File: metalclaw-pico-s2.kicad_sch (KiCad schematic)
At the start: 3 parts, among them J1 USB_C_Receptacle_USB2.0_14P, U1 ESP32-S2, U2 W25Q16JVSS

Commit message: Initial schematic connections
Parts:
- added A2: RaspberryPi_Pico, Module:RaspberryPi_Pico_SMD_HandSolder, symbol MCU_Module:RaspberryPi_Pico_Debug
- added C1, C2, C3: C, symbol Device:C
- added R1, R29, R30, R31, R32, R33, R34, R35: 5.1k, symbol Device:R_US
- added R10, R11, R12, R13, R14, R15, R16, R17, R18, R19, R2, R20, R21, R22, R23, R24, R25, R26, R27, R28, R3, R4, R5, R6, R7, R8, R9: R_US, symbol Device:R_US
- added U3: APS6404L-3SQRx-SN, Package_SO:SOIC-8_3.9x4.9mm_P1.27mm, symbol Memory_RAM:APS6404L-3SQRx-SN
- added U4: AMS1117-3.3, Package_TO_SOT_SMD:SOT-223-3_TabPin2, symbol Regulator_Linear:AMS1117-3.3
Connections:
- net GND: now also U1.57 (GND), U2.4 (GND), A2.13 (GND), A2.18 (GND), A2.23 (GND), A2.28 (GND), A2.3 (GND), A2.33 (AGND), A2.38 (GND), A2.8 (GND), A2.D2 (GND), C1.2, C2.2, C3.2, R1.1, R29.1, R30.1, R31.1, U3.4 (VSS), U4.1 (GND)
- net VBUS: now reaches J1.A4 (VBUS), J1.A9 (VBUS), J1.B4 (VBUS), J1.B9 (VBUS)
- net VBUS: now also A2.40 (VBUS), C1.1, U4.3 (VI)
- net at J1.A5 (CC1): now also R1.2
- net at J1.A6 (D+), U1.26 (GPIO20/USB_D+): no longer J1.B6 (D+)
- net at J1.B5 (CC2): now also R29.2
- net GP4: now reaches U1.10 (GPIO5)
- net GP4: now also R6.2
- net GP5: now reaches U1.11 (GPIO6)
- net GP5: now also R7.2
- net GP6: now reaches U1.12 (GPIO7)
- net GP6: now also R18.2, R34.2
- net GP7: now reaches U1.13 (GPIO8)
- net GP7: now also R19.2, R35.2
- net GP8: now reaches U1.14 (GPIO9)
- net GP8: now also R20.2
- net GP9: now reaches U1.15 (GPIO10)
- net GP9: now also R21.2
- net GP10: now reaches U1.16 (GPIO11)
- net GP10: now also R22.2
- net GP11: now reaches U1.17 (GPIO12)
- net GP11: now also R23.2
- net GP12: now reaches U1.18 (GPIO13)
- net GP12: now also R24.2
- net GP13: now reaches U1.19 (GPIO14)
- net GP13: now also R25.2
- net GP14: now reaches U1.21 (XTAL_32K_P)
- net GP14: now also R26.2
- net GP15: now reaches U1.22 (XTAL_32K_N)
- net GP15: now also R27.2
- net GP26: now reaches U1.23 (DAC_1)
- net GP26: now also R8.2
- net GP27: now reaches U1.24 (DAC_2)
- net GP27: now also R16.2
- net at U1.28 (GPIO21): now also R28.1
- net at U1.29 (SPICS1): now also U3.1 (~{CE})
- net at U1.31 (SPIHD), U2.7 (~{HOLD}/~{RESET}/IO_{3}): now also U3.3 (SIO2)
- net at U1.32 (SPIWP), U2.3 (~{WP}/IO_{2}): now also U3.7 (SIO3)
- net at U1.34 (SPICLK), U2.6 (CLK): now also U3.6 (SCLK)
- net at U1.35 (SPIQ): now also U2.5 (DI/IO_{0}), U3.5 (SI/SIO0)
- net at U1.36 (SPID): now also U2.2 (DO/IO_{1}), U3.2 (SO/SIO1)
- net GP16: now reaches U1.37 (GPIO33)
- net GP16: now also R15.2
- net GP17: now reaches U1.38 (GPIO34)
- net GP17: now also R14.2
- net GP18: now reaches U1.39 (GPIO35)
- net GP18: now also R13.2
- net GP19: now reaches U1.40 (GPIO36)
- net GP19: now also R12.2
- net GP21: now reaches U1.41 (GPIO37)
- net GP21: now also R10.2, R33.2
- net GP20: now reaches U1.42 (GPIO38)
- net GP20: now also R11.2, R32.2
- net SWCLK: now reaches U1.48 (U0TXD)
- net SWCLK: now also A2.D1 (SWCLK)
- net SWDIO: now reaches U1.49 (U0RXD)
- net SWDIO: now also A2.D3 (SWDIO)
- net RUN: now reaches U1.5 (GPIO0)
- net RUN: now also A2.30 (RUN)
- net 3V3_EN: now reaches U1.50 (GPIO45)
- net 3V3_EN: now also A2.37 (3V3_EN), R30.2
- net GP22: now reaches U1.55 (GPIO46)
- net GP22: now also R31.2, R9.2
- net GP0: now reaches U1.6 (GPIO1)
- net GP0: now also R2.2
- net GP1: now reaches U1.7 (GPIO2)
- net GP1: now also R3.2
- net GP2: now reaches U1.8 (GPIO3)
- net GP2: now also R4.2
- net GP3: now reaches U1.9 (GPIO4)
- net GP3: now also R5.2
- net +3.3V: now reaches U2.8 (VCC)
- net +3.3V: now also U3.8 (VDD)
- new net: A2.16 (GPIO12), R24.1
- new net: A2.1 (GPIO0), R2.1
- new net: A2.10 (GPIO7), R19.1
- new net: A2.11 (GPIO8), R20.1
- new net: A2.12 (GPIO9), R21.1
- new net: A2.14 (GPIO10), R22.1
- new net: A2.15 (GPIO11), R23.1
- new net: A2.17 (GPIO13), R25.1
- new net: A2.19 (GPIO14), R26.1
- new net: A2.2 (GPIO1), R3.1
- new net: A2.20 (GPIO15), R27.1
- new net: A2.21 (GPIO16), R15.1
- new net: A2.22 (GPIO17), R14.1
- new net: A2.24 (GPIO18), R13.1
- new net: A2.25 (GPIO19), R12.1
- new net: A2.26 (GPIO20), R11.1
- new net: A2.27 (GPIO21), R10.1
- new net: A2.29 (GPIO22), R9.1
- new net: A2.31 (GPIO26_ADC0), R8.1
- new net: A2.32 (GPIO27_ADC1), R16.1
- new net: A2.34 (GPIO28_ADC2), R17.1
- new net: A2.4 (GPIO2), R4.1
- new net: A2.5 (GPIO3), R5.1
- new net: A2.6 (GPIO4), R6.1
- new net: A2.7 (GPIO5), R7.1
- new net: A2.9 (GPIO6), R18.1
- new net +3V3: A2.35 (ADC_VREF), A2.36 (3V3), C3.1, R32.1, R33.1, R34.1, R35.1, U4.2 (VO)
- new net GP28: C2.1, J1.B6 (D+), R17.2, R28.2
- new net VS: A2.39 (VSYS)
- no-connect marks 1 -> 2
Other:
- moved on the sheet: J1, U1, U2

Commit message: Switch 3V3_EN and RUN pins
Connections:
- net 3V3_EN: now also U1.5 (GPIO0); no longer R30.2, U1.50 (GPIO45)
- net RUN: now also R30.2, U1.50 (GPIO45); no longer U1.5 (GPIO0)
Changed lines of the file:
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@@
 	)
 	(label "3V3_EN"
-		(at 121.92 53.34 270)
+		(at 71.12 147.32 90)
 		(effects
 			(font
 				(size 1.27 1.27)
 			)
-			(justify right bottom)
+			(justify left bottom)
 		)
 	)
@@
 	)
 	(label "RUN"
-		(at 71.12 147.32 90)
+		(at 121.92 53.34 270)
 		(effects
 			(font
 				(size 1.27 1.27)
 			)
-			(justify left bottom)
+			(justify right bottom)
 		)
 	)

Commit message: Specify series resistor resistance and footprint
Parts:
- removed R17: R_US, symbol Device:R_US
- R1, R29, R30, R31, R32, R33, R34, R35: footprint (none) -> Capacitor_SMD:C_0402_1005Metric
- R10, R11, R12, R13, R14, R15, R16, R18, R19, R2, R20, R21, R22, R23, R24, R25, R26, R27, R28, R3, R4, R5, R6, R7, R8, R9: value R_US -> 220; footprint (none) -> Capacitor_SMD:C_0402_1005Metric
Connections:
- net GP28: now also A2.34 (GPIO28_ADC2)

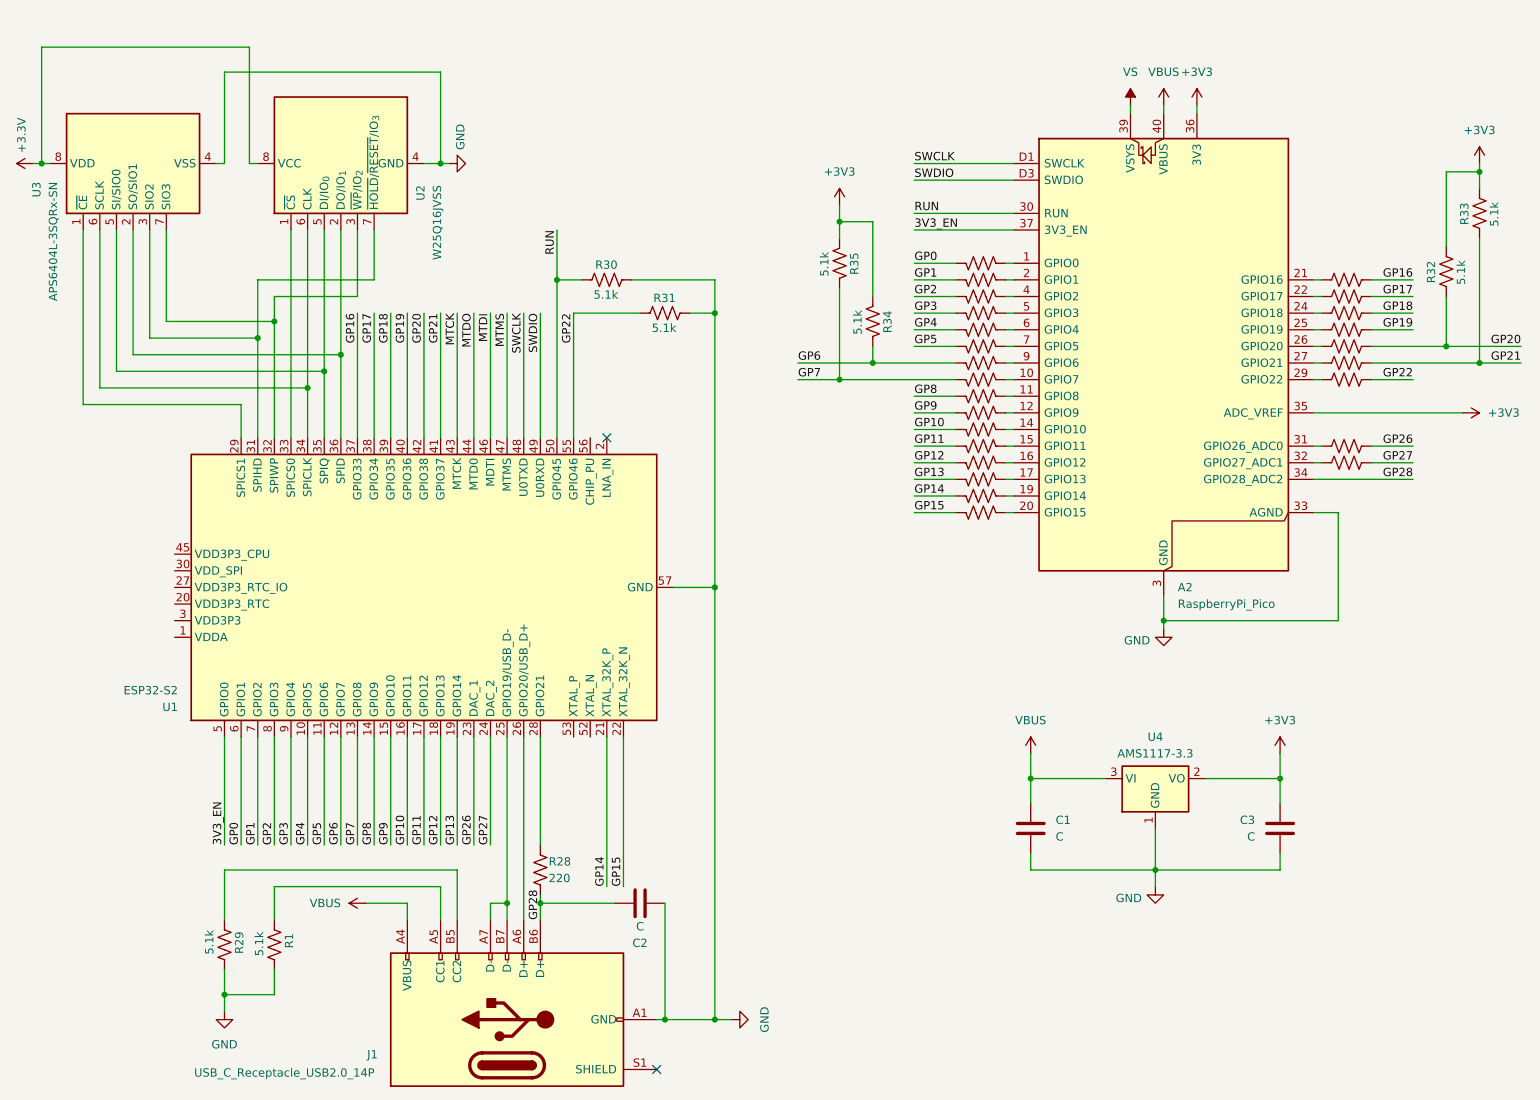
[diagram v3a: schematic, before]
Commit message: Add cap banks to ESP32-S2
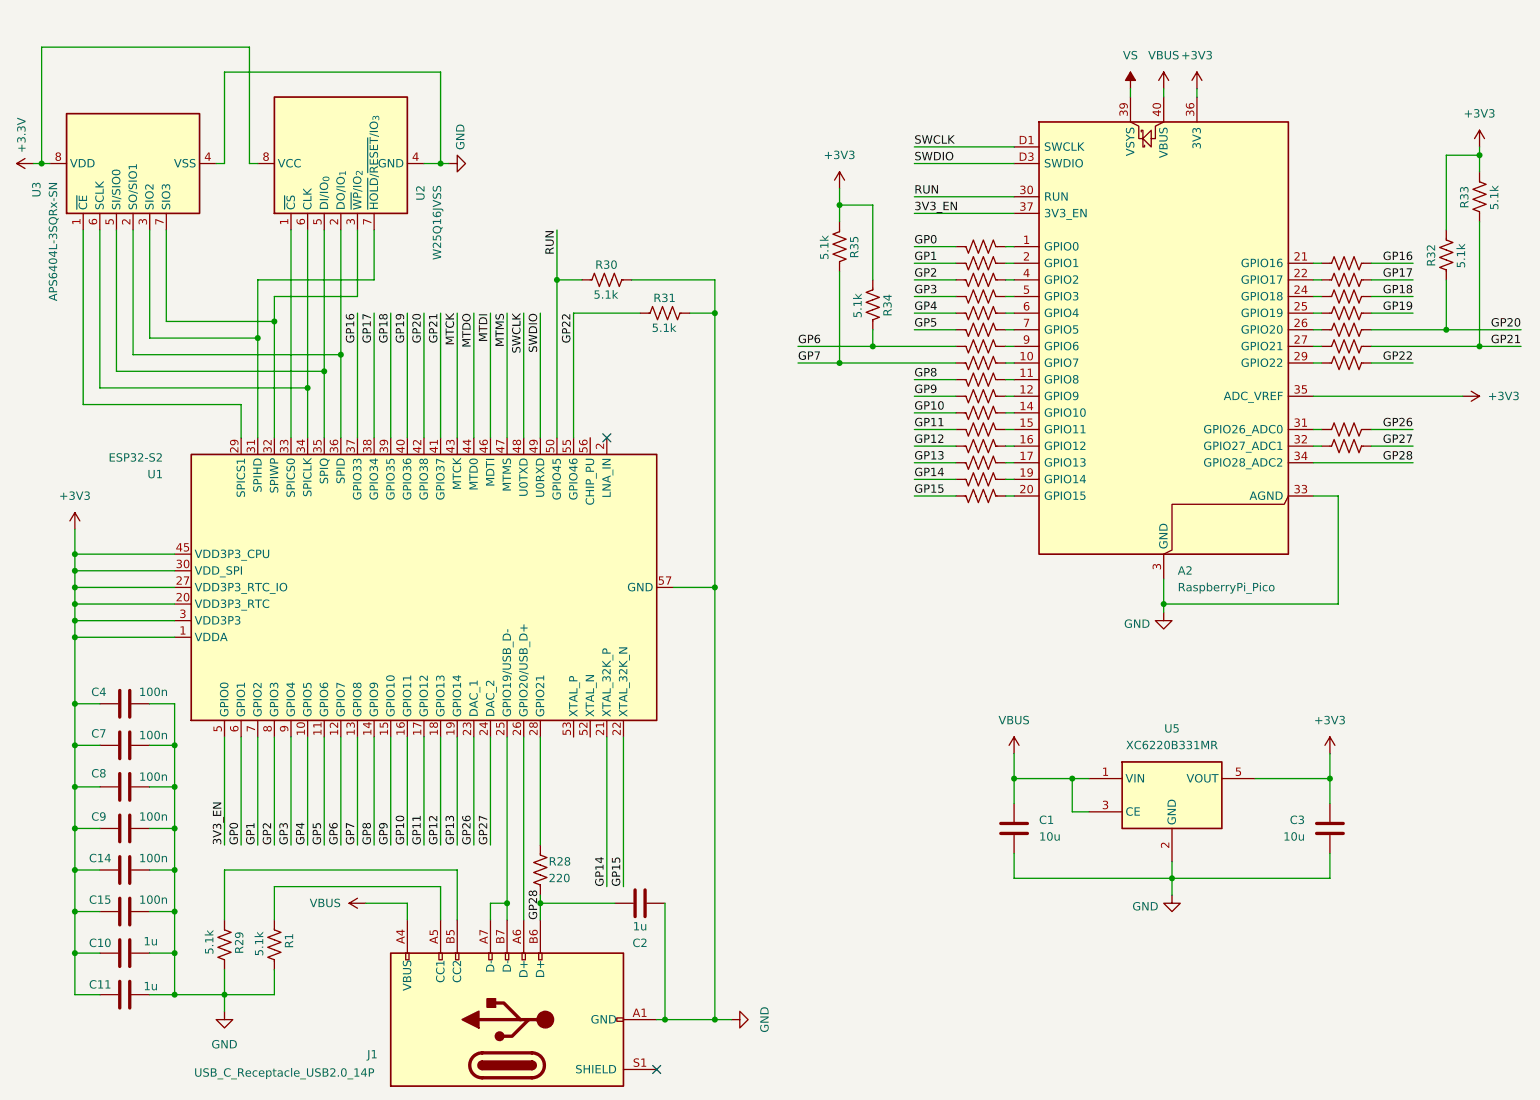
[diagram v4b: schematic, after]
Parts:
- removed U4: AMS1117-3.3, Package_TO_SOT_SMD:SOT-223-3_TabPin2, symbol Regulator_Linear:AMS1117-3.3
- added C10, C11: 1u, symbol Device:C
- added C14, C15, C4, C7, C8, C9: 100n, symbol Device:C
- added U5: XC6220B331MR, Package_TO_SOT_SMD:SOT-23-5, symbol Regulator_Linear:XC6220B331MR
- C1, C3: value C -> 10u
- C2: value C -> 1u
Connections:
- net +3V3: now also U1.1 (VDDA), U1.20 (VDD3P3_RTC), U1.27 (VDD3P3_RTC_IO), U1.3 (VDD3P3), U1.30 (VDD_SPI), U1.4 (VDD3P3), U1.45 (VDD3P3_CPU), U1.51 (VDDA), U1.54 (VDDA), C10.1, C11.1, C14.1, C15.1, C4.1, C7.1, C8.1, C9.1, U5.5 (VOUT)
- net GND: now also C10.2, C11.2, C14.2, C15.2, C4.2, C7.2, C8.2, C9.2, U5.2 (GND)
- net VBUS: now also U5.1 (VIN), U5.3 (CE)
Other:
- moved on the sheet: A2, C1, C3, R32, R33, R34, R35

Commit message: Add crystal
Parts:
- added C5, C6: 6p, symbol Device:C
- added Y1: XRCGB40M000F1S2FR0, Crystal:Crystal_SMD_2016-4Pin_2.0x1.6mm, symbol Device:Crystal_GND24
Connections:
- net GND: now also C5.2, C6.2, Y1.2 (G), Y1.4 (G)
- net at U1.52 (XTAL_N): now also C6.1, Y1.3
- net at U1.53 (XTAL_P): now also C5.1, Y1.1

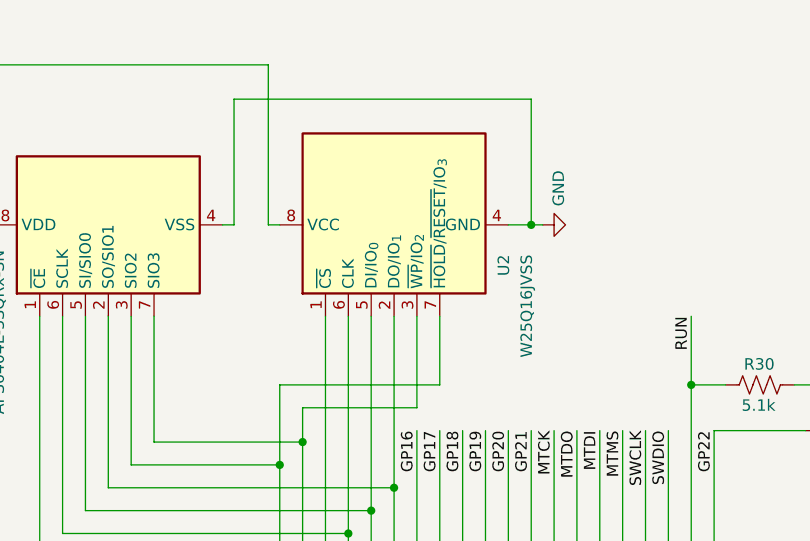
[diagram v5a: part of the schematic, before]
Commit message: Specify SPI flash part and footprint
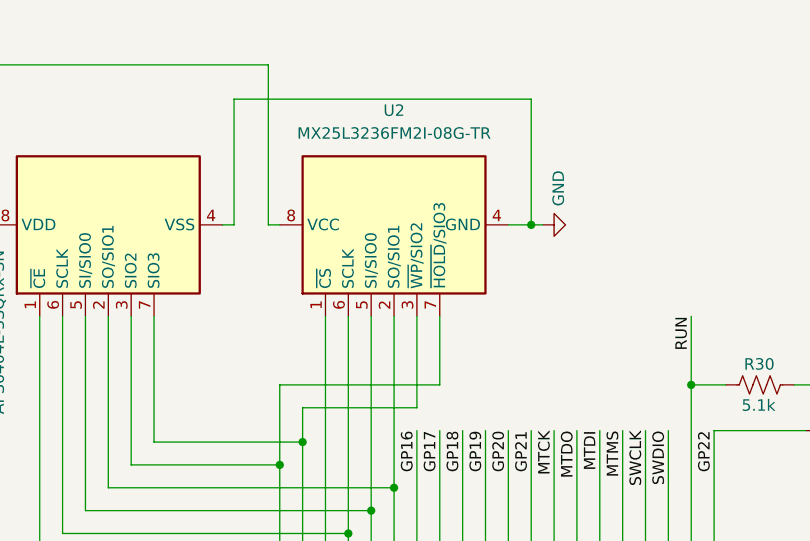
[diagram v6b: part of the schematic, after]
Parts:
- removed U2: W25Q16JVSS, Package_SO:SOIC-8_5.3x5.3mm_P1.27mm, symbol Memory_Flash:W25Q16JVSS
- added U2: MX25L3236FM2I-08G-TR, Package_SO:SOIC-8_5.3x5.3mm_P1.27mm, symbol Memory_Flash:MX25L3233FM2
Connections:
- net +3.3V: now also U2.8 (VCC)
- net GND: now also U2.4 (GND)
- net at U1.31 (SPIHD), U3.3 (SIO2): now also U2.7 (~{HOLD}/SIO3)
- net at U1.32 (SPIWP), U3.7 (SIO3): now also U2.3 (~{WP}/SIO2)
- net at U1.33 (SPICS0): now also U2.1 (~{CS})
- net at U1.34 (SPICLK), U3.6 (SCLK): now also U2.6 (SCLK)
- net at U1.35 (SPIQ), U3.5 (SI/SIO0): now also U2.5 (SI/SIO0)
- net at U1.36 (SPID), U3.2 (SO/SIO1): now also U2.2 (SO/SIO1)
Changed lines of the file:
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@@
+	)
+	(symbol
+		(lib_id "Memory_Flash:MX25L3233FM2")
+		(at 88.9 43.18 90)
+		(unit 1)
+		(exclude_from_sim no)
+		(in_bom yes)
+		(on_board yes)
+		(dnp no)
+		(fields_autoplaced yes)
+		(property "Reference" "U2"
+			(at 88.9 30.48 90)
+			(effects
+				(font
+					(size 1.27 1.27)
+				)
+			)
+		)
+		(property "Value" "MX25L3236FM2I-08G-TR"
+			(at 88.9 33.02 90)
+			(effects
+				(font
+					(size 1.27 1.27)
+				)
+			)
+		)
+		(property "Footprint" "Package_SO:SOIC-8_5.3x5.3mm_P1.27mm"
+			(at 104.14 43.18 0)
+			(effects
+				(font
+					(size 1.27 1.27)
+				)
+				(hide yes)
+			)
+		)
+		(property "Datasheet" "https://www.macronix.com/Lists/Datasheet/Attachments/8933/MX25L3233F,%203V,%2032Mb,%20v1.7.pdf"
+			(at 106.426 43.18 0)
+			(effects
+				(font
+					(size 1.27 1.27)
+				)
+				(hide yes)
+			)
+		)
+		(property "Description" "32-Mbit, 3V (2.65V-3.6V) SPI Serial Flash Memory, SOIC-8 (SOP-8, 208 mil)"
+			(at 88.9 43.18 0)
+			(effects
+				(font
+					(size 1.27 1.27)
+				)
+				(hide yes)
+			)
+		)
+		(pin "1"
+		)
+		(pin "6"
+		)
+		(pin "5"
+		)
+		(pin "2"
+		)
+		(pin "3"
+		)
+		(pin "7"
+		)
+		(pin "8"
+		)
+		(pin "4"
+		)
+		(instances
+			(project ""
+				(path "/c83ebc88-59c8-491c-acdb-d3cfac2d55f0"
+					(reference "U2")
+					(unit 1)
+				)
+			)
+		)
 	)
 	(symbol
@@
 					(unit 1)
 				)
-			)
-		)
-	)
-	(symbol
-		(lib_id "Memory_Flash:W25Q16JVSS")
-		(at 88.9 43.18 90)
-		(unit 1)
-		(exclude_from_sim no)
-		(in_bom yes)
-		(on_board yes)
-		(dnp no)
-		(property "Reference" "U2"
-			(at 101.092 46.482 0)
-			(effects
-				(font
-					(size 1.27 1.27)
-				)
-				(justify right)
-			)
-		)
-		(property "Value" "W25Q16JVSS"
-			(at 103.632 46.482 0)
-			(effects
-				(font
-					(size 1.27 1.27)
-				)
-				(justify right)
-			)
-		)
-		(property "Footprint" "Package_SO:SOIC-8_5.3x5.3mm_P1.27mm"
-			(at 88.9 43.18 0)
-			(effects
-				(font
-					(size 1.27 1.27)
-				)
-				(hide yes)
-			)
-		)
-		(property "Datasheet" "https://www.winbond.com/hq/support/documentation/levelOne.jsp?__locale=en&DocNo=DA00-W25Q16JV.1"
-			(at 88.9 43.18 0)
-			(effects
-				(font
-					(size 1.27 1.27)
-				)
-				(hide yes)
-			)
-		)
-		(property "Description" "16Mbit / 2MiB Serial Flash Memory, Standard/Dual/Quad SPI, 2.7-3.6V, SOIC-8 (208 mil)"
-			(at 88.9 43.18 0)
-			(effects
-				(font
-					(size 1.27 1.27)
-				)
-				(hide yes)
-			)
-		)
-		(pin "5"
-		)
-		(pin "4"
-		)
-		(pin "3"
-		)
-		(pin "8"
-		)
-		(pin "7"
-		)
-		(pin "1"
-		)
-		(pin "6"
-		)
-		(pin "2"
-		)
-		(instances
-			(project ""
-				(path "/c83ebc88-59c8-491c-acdb-d3cfac2d55f0"
-					(reference "U2")
-					(unit 1)
-				)
